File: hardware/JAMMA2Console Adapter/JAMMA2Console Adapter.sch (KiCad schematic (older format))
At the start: 3 parts, among them J1 KF141R-2.54-7P, J2 KF141R-2.54-7P, J4 DS1037-15MNCKT74-0CC

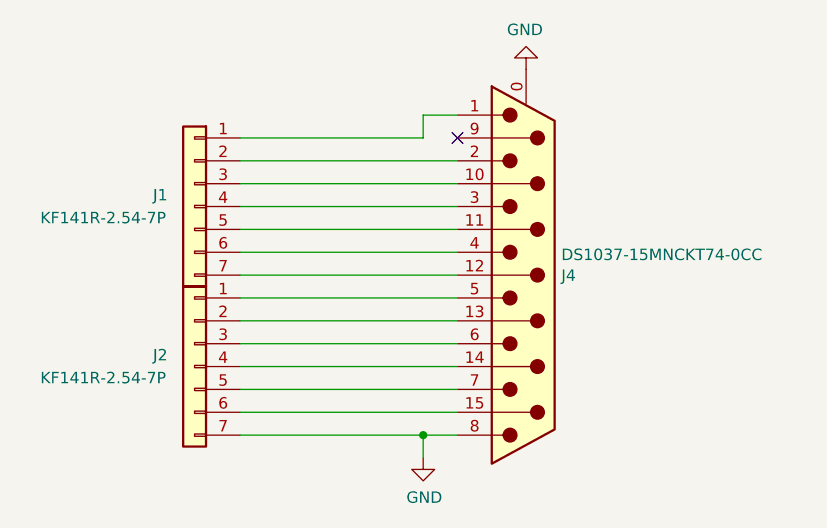
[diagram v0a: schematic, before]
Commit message: Started major rework on the Audio section (chose the wrong amplifier as it can't drive 4Ohm loads) Moved over to nightly Kicad v 5.9 versions. Was a mistake to do, but will look into reverting another time.
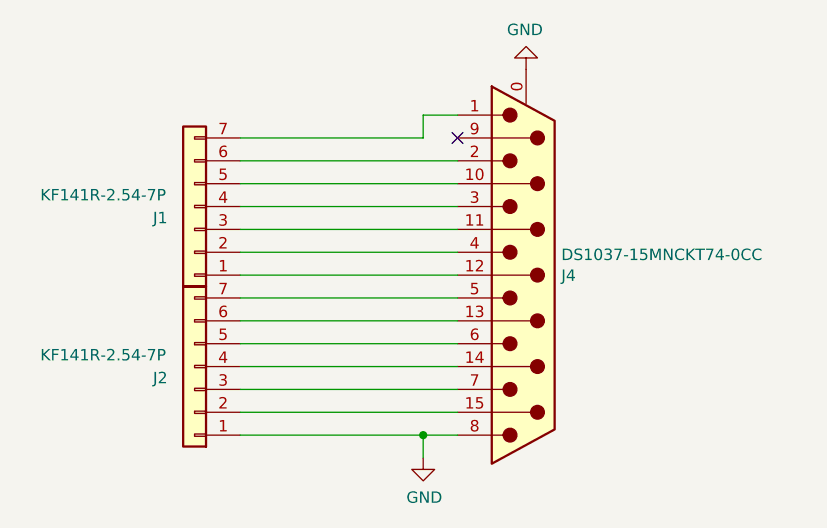
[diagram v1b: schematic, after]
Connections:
- net GND: now also J2.1 (Pin_1); no longer J2.7 (Pin_7)
- net at J4.1: now also J1.7 (Pin_7); no longer J1.1 (Pin_1)
- net at J4.10 (P10): now also J1.5 (Pin_5); no longer J1.3 (Pin_3)
- net at J4.11 (P111): now also J1.3 (Pin_3); no longer J1.5 (Pin_5)
- net at J4.12 (P12): now also J1.1 (Pin_1); no longer J1.7 (Pin_7)
- net at J4.13 (P13): now also J2.6 (Pin_6); no longer J2.2 (Pin_2)
- net at J4.15 (P15): now also J2.2 (Pin_2); no longer J2.6 (Pin_6)
- net at J4.2: now also J1.6 (Pin_6); no longer J1.2 (Pin_2)
- net at J4.4: now also J1.2 (Pin_2); no longer J1.6 (Pin_6)
- net at J4.5: now also J2.7 (Pin_7); no longer J2.1 (Pin_1)
- net at J4.6: now also J2.5 (Pin_5); no longer J2.3 (Pin_3)
- net at J4.7: now also J2.3 (Pin_3); no longer J2.5 (Pin_5)
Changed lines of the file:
@@
 F 3 "~" H 4500 2500 50  0001 C CNN
 	1    4500 2500
-	-1   0    0    -1
+	-1   0    0    1
 $EndComp
 $Comp
@@
 F 3 "~" H 4500 3200 50  0001 C CNN
 	1    4500 3200
-	-1   0    0    -1
+	-1   0    0    1
 $EndComp
 Wire Wire Line
